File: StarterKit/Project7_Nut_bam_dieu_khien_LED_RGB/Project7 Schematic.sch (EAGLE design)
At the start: 6 parts, among them U1 ARDUINOR3-BPLACE

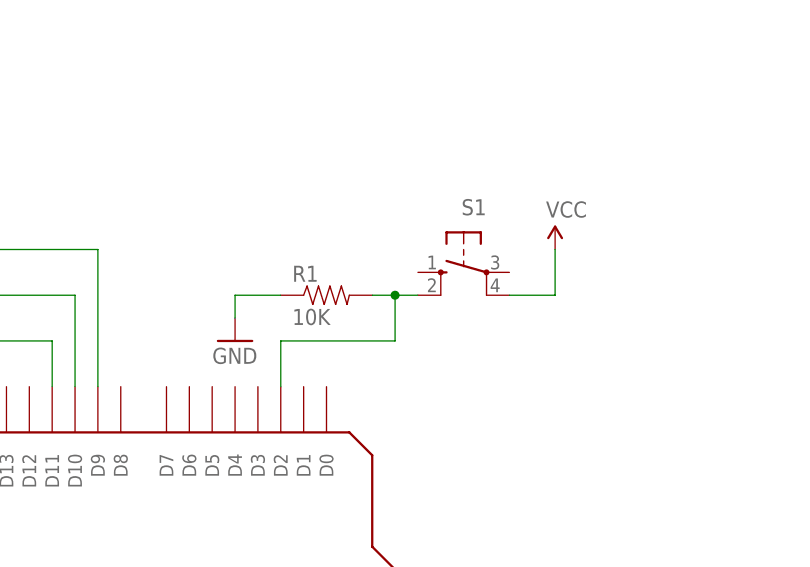
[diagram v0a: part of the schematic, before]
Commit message: Chuyen tu dien tro keo thap (pull-down) sang keo cao (pull-up) cho project 1a,1b,1c,7,11.
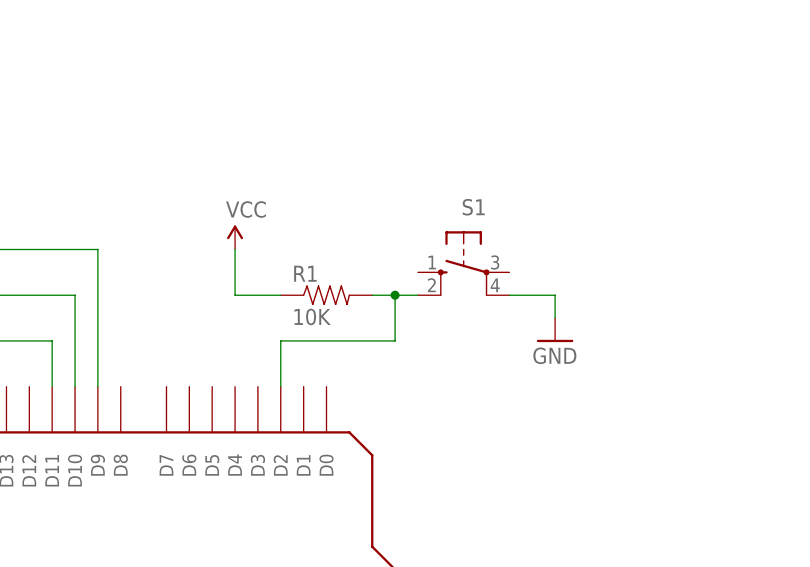
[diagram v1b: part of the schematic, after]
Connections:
- net GND: now also S1.P1; no longer R1.1
- net VCC: now also R1.1; no longer S1.P1
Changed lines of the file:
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@@
 <instance part="R2" gate="G$1" x="27.94" y="119.38"/>
 <instance part="S1" gate="1" x="114.3" y="121.92" rot="MR270"/>
-<instance part="GND3" gate="1" x="88.9" y="114.3"/>
-<instance part="SUPPLY2" gate="G$1" x="124.46" y="124.46"/>
+<instance part="GND3" gate="1" x="124.46" y="114.3"/>
+<instance part="SUPPLY2" gate="G$1" x="88.9" y="124.46"/>
 <instance part="FRAME1" gate="G$1" x="-33.02" y="-15.24"/>
 <instance part="FRAME1" gate="V" x="114.3" y="-15.24"/>
@@
 </segment>
 <segment>
-<pinref part="S1" gate="1" pin="P1"/>
-<pinref part="SUPPLY2" gate="G$1" pin="VCC"/>
-<wire x1="119.38" y1="119.38" x2="124.46" y2="119.38" width="0.1524" layer="91"/>
-<wire x1="124.46" y1="119.38" x2="124.46" y2="124.46" width="0.1524" layer="91"/>
-</segment>
-<segment>
 <pinref part="SUPPLY3" gate="G$1" pin="VCC"/>
 <wire x1="20.32" y1="127" x2="20.32" y2="119.38" width="0.1524" layer="91"/>
 <pinref part="R2" gate="G$1" pin="1"/>
 <wire x1="20.32" y1="119.38" x2="22.86" y2="119.38" width="0.1524" layer="91"/>
+</segment>
+<segment>
+<pinref part="SUPPLY2" gate="G$1" pin="VCC"/>
+<wire x1="88.9" y1="124.46" x2="88.9" y2="119.38" width="0.1524" layer="91"/>
+<pinref part="R1" gate="G$1" pin="1"/>
+<wire x1="88.9" y1="119.38" x2="93.98" y2="119.38" width="0.1524" layer="91"/>
 </segment>
 </net>
@@
 </segment>
 <segment>
+<pinref part="S1" gate="1" pin="P1"/>
 <pinref part="GND3" gate="1" pin="GND"/>
-<wire x1="88.9" y1="116.84" x2="88.9" y2="119.38" width="0.1524" layer="91"/>
-<pinref part="R1" gate="G$1" pin="1"/>
-<wire x1="88.9" y1="119.38" x2="93.98" y2="119.38" width="0.1524" layer="91"/>
+<wire x1="119.38" y1="119.38" x2="124.46" y2="119.38" width="0.1524" layer="91"/>
+<wire x1="124.46" y1="119.38" x2="124.46" y2="116.84" width="0.1524" layer="91"/>
 </segment>
 </net>
